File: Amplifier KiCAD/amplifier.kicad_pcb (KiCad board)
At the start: 2 copper layers, 197 parts, among them J1 Conn_01x03_Pin, J10 PA_IN, J11 EQ_OUT, J12 Speakers, J2 Main Power In, J3 LCD I2C, J4 Fan Tach and PWM, J5 Fan Power and GND, J6 VP and VN, J7 DEBUG, J8 Power To Amp, J9 Power In, Q1 BC546, Q10 TIP36, Q11 BC546, Q12 BCM846BS-7, Q13 BC546, Q14 BC546, Q15 BD140, Q16 BC546, Q17 BD139, Q18 BD140, Q19 TIP36, Q2 BC546, Q20 TIP35, Q21 2N3904, Q22 2N7002, Q3 BCM846BS-7, Q4 BC546, Q5 BD140, Q6 BC546, Q7 BD140, Q8 TIP35, Q9 BD139, SW1 SW_Push, U1 TL081, U10 LM317_TO-220, U11 LM337_TO220, U12 STM32G031K8Tx, U2 TL081, U3 TL081, U4 TL081, U5 TL081, U6 TL081, U7 LMR36520FADDAR, U8 LMR36520FADDAR, U9 TLV75533PDBVR

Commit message: Component Placement Finalised, Starting Traces
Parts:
- removed Q12, Q3: BCM846BS-7, Package_TO_SOT_SMD:SOT-363_SC-70-6
- added Q23: BCM846BS-7, Package_TO_SOT_SMD:SOT-363_SC-70-6, F.Cu at (103.5, -152.4)
- added Q24: BCM846BS-7, Package_TO_SOT_SMD:SOT-363_SC-70-6, F.Cu at (100.8, -116.2)
- added REF**: MountingHole_3.2mm_M3, MountingHole:MountingHole_3.2mm_M3, F.Cu at (330.8, -118.7)
- added REF**: MountingHole_3.2mm_M3, MountingHole:MountingHole_3.2mm_M3, F.Cu at (228.0, -81.3)
- added REF**: MountingHole_3.2mm_M3, MountingHole:MountingHole_3.2mm_M3, F.Cu at (330.8, -87.6)
- added REF**: MountingHole_3.2mm_M3, MountingHole:MountingHole_3.2mm_M3, F.Cu at (69.8, -172.7)
- added REF**: MountingHole_3.2mm_M3, MountingHole:MountingHole_3.2mm_M3, F.Cu at (515.0, -118.7)
- added REF**: MountingHole_3.2mm_M3, MountingHole:MountingHole_3.2mm_M3, F.Cu at (228.0, -172.1)
- added REF**: MountingHole_3.2mm_M3, MountingHole:MountingHole_3.2mm_M3, F.Cu at (69.8, -81.3)
- added REF**: MountingHole_3.2mm_M3, MountingHole:MountingHole_3.2mm_M3, F.Cu at (515.0, -87.6)
- J5: footprint Connector_Molex:Molex_Micro-Fit_3.0_43045-0812_2x04_P3.00mm_Vertical -> KiCADModels:Molex_Micro-Fit_3.0_43045-0812_2x04_P3.00mm_Vertical
- moved RV8 466.1 mm to (463.4, -90.3), turned to 90 degrees
- moved J4 438.5 mm to (480.3, -116.8)
- moved RV7 437.1 mm to (436.1, -90.3), turned to 90 degrees
- moved J5 428.0 mm to (461.7, -117.0)
- moved RV6 410.0 mm to (410.8, -90.3), turned to 90 degrees
- moved RV5 381.1 mm to (383.5, -90.3), turned to 90 degrees
- moved J8 355.1 mm to (378.0, -120.8), turned to 180 degrees
- moved J1 322.7 mm to (354.8, -85.1), turned to 90 degrees
- moved J12 282.3 mm to (225.1, -125.7), turned to 90 degrees
- moved R27 268.0 mm to (175.9, -161.9), turned to 90 degrees
- moved J10 262.3 mm to (76.8, -150.9), turned to 90 degrees
- moved Q8 260.1 mm to (184.0, -172.5), turned to -90 degrees
- moved C11 257.4 mm to (-92.0, 97.3)
- moved C12 257.4 mm to (-92.0, 100.2)
- moved C18 257.4 mm to (-81.9, 131.5)
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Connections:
- R20 pad 2: VCC -> Net-(Q10-E)
- R35 pad 2: VCC -> Net-(Q14-C)
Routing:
- net Out+: track 0.00 -> 137.4 mm
- net VCC: track 0.00 -> 69.9 mm
- net Net-(Q1-C): track 0.00 -> 35.0 mm
- net VEE: track 0.00 -> 33.3 mm
- net Net-(Q6-E): track 0.00 -> 29.8 mm
- net Net-(Q2-B): track 0.00 -> 24.8 mm
- net Net-(Q23B-C2): track 0.00 -> 22.8 mm
- net Net-(Q14-B): track 0.00 -> 22.5 mm
- net Net-(Q13-B): track 0.00 -> 22.3 mm
- net Net-(Q5-C): track 0.00 -> 20.2 mm
- net Net-(C29-Pad2): track 0.00 -> 20.1 mm
- net Net-(Q6-B): track 0.00 -> 18.8 mm
- net Net-(Q23A-E1): track 0.00 -> 18.7 mm, vias 0 -> 3
- net In+: track 0.00 -> 17.9 mm
- net Net-(C39-Pad2): track 0.00 -> 17.3 mm
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- added copper zone on In1.Cu, net Net-(Q10-E)
- added copper zone on In1.Cu, net Net-(Q14-C)
- added copper zone on In2.Cu, net Net-(Q20-E)
- added copper zone on In2.Cu, net Net-(Q23A-E1)
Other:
- board outline added: 454.3 x 100.3 mm
- copper layers 2 -> 4

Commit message: Save Before big changes
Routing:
- net Out+: track 137.4 -> 0.00 mm
- net VCC: track 69.9 -> 0.00 mm
- net Net-(Q1-C): track 35.0 -> 0.00 mm
- net VEE: track 33.3 -> 0.00 mm
- net Net-(Q6-E): track 29.8 -> 0.00 mm
- net Net-(Q2-B): track 24.8 -> 0.00 mm
- net Net-(Q23B-C2): track 22.8 -> 0.00 mm
- net Net-(Q14-B): track 22.5 -> 0.00 mm
- net Net-(Q13-B): track 22.3 -> 0.00 mm
- net Net-(Q5-C): track 20.2 -> 0.00 mm
- net Net-(C29-Pad2): track 20.1 -> 0.00 mm
- net Net-(Q6-B): track 18.8 -> 0.00 mm
- net Net-(Q23A-E1): track 18.7 -> 0.00 mm, vias 3 -> 0
- net In+: track 17.9 -> 0.00 mm
- net Net-(C39-Pad2): track 17.3 -> 0.00 mm
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
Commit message: Save before KiCAD update
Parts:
- moved J11 524.9 mm to (383.1, -118.9)
- moved C27 295.3 mm to (123.6, 149.6), turned to 90 degrees
- moved R16 290.4 mm to (118.4, 150.0), turned to 90 degrees
- moved R15 285.6 mm to (113.5, 139.8), turned to -90 degrees
- moved U11 284.7 mm to (102.7, 146.1)
- moved D3 280.7 mm to (108.2, 154.6), turned to 180 degrees
- moved D4 280.1 mm to (108.2, 149.7), turned to 180 degrees
- moved C23 279.0 mm to (116.3, 152.9), turned to 180 degrees
- moved C26 261.2 mm to (89.5, 154.6)
- moved C22 254.9 mm to (92.3, 151.4)
- moved RFBT2 235.4 mm to (137.3, 100.5), turned to 180 degrees
- moved C17 235.3 mm to (37.5, 82.0)
- moved C20 235.3 mm to (18.0, 96.2)
- moved C21 235.3 mm to (37.5, 84.9)
- moved C24 235.3 mm to (28.4, 82.5)
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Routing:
- net GND: track 0.00 -> 279.8 mm
- net VCC: track 0.00 -> 218.7 mm
- net Net-(Q14-C): track 0.00 -> 197.1 mm
- net Net-(Q23A-E1): track 0.00 -> 194.4 mm, vias 0 -> 3
- net VEE: track 0.00 -> 168.9 mm
- net Net-(Q20-E): track 0.00 -> 168.7 mm, vias 0 -> 2
- net Net-(Q10-E): track 0.00 -> 148.4 mm
- net Out+: track 0.00 -> 118.1 mm
- net Out-: track 0.00 -> 114.0 mm
- net Net-(Q17-E): track 0.00 -> 57.5 mm
- net Net-(Q10-C): track 0.00 -> 53.4 mm
- net Net-(Q18-C): track 0.00 -> 50.7 mm
- net Net-(Q10-B): track 0.00 -> 50.5 mm
- net Net-(Q17-C): track 0.00 -> 48.4 mm
- net Net-(Q18-E): track 0.00 -> 44.5 mm
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- removed copper zone on In1.Cu, net Net-(Q10-E)
- removed copper zone on In1.Cu, net Net-(Q14-C)
- removed copper zone on In2.Cu, net Net-(Q20-E)
- removed copper zone on In2.Cu, net Net-(Q23A-E1)

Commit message: Completed placement of equaliser; Tidied up soldermask; Started STM32 placement
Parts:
- moved R12 615.8 mm to (402.6, 76.8), turned to 180 degrees
- moved R11 606.0 mm to (391.8, 61.6)
- moved R9 583.9 mm to (370.4, 61.2), turned to -90 degrees
- moved R10 580.1 mm to (367.1, 70.9), turned to 180 degrees
- moved U3 577.4 mm to (389.9, 72.9), turned to 180 degrees
- moved R7 556.5 mm to (343.3, 58.5), turned to -90 degrees
- moved C16 555.9 mm to (377.6, 71.2), turned to 90 degrees
- moved U6 554.5 mm to (401.7, 72.8), turned to 180 degrees
- moved R8 553.0 mm to (340.3, 68.3), turned to 180 degrees
- moved C13 552.9 mm to (365.5, 74.7)
- moved C14 551.9 mm to (373.9, 71.2), turned to 90 degrees
- moved C59 543.6 mm to (373.9, 58.1), turned to -90 degrees
- moved C9 534.2 mm to (346.9, 68.5), turned to 90 degrees
- moved C58 533.0 mm to (354.1, 71.0), turned to 90 degrees
- moved C10 533.0 mm to (345.8, 76.5), turned to 90 degrees
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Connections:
- RV5 pad 1: GND -> Net-(U3-+)
- RV5 pad 2: Bass -> Net-(C3-Pad2)
- RV5 pad 3: +3.3V -> Net-(U3--)
- RV5 pad 4: Net-(U3--) -> GND
- RV5 pad 5: Net-(C3-Pad2) -> Bass
- RV5 pad 6: Net-(U3-+) -> +3.3V
- RV6 pad 1: GND -> Net-(U3-+)
- RV6 pad 2: Mid -> Net-(C10-Pad1)
- RV6 pad 3: +3.3V -> Net-(U3--)
- RV6 pad 4: Net-(U3--) -> GND
- RV6 pad 5: Net-(C10-Pad1) -> Mid
- RV6 pad 6: Net-(U3-+) -> +3.3V
- RV7 pad 1: GND -> Net-(U3-+)
- RV7 pad 2: Treble -> Net-(C13-Pad1)
- RV7 pad 3: +3.3V -> Net-(U3--)
- RV7 pad 4: Net-(U3--) -> GND
- RV7 pad 5: Net-(C13-Pad1) -> Treble
- RV7 pad 6: Net-(U3-+) -> +3.3V
- RV8 pad 1: GND -> In+
- RV8 pad 2: Volume -> Net-(U3--)
- RV8 pad 3: +3.3V -> unconnected-(RV8-Pad3)
- RV8 pad 4: unconnected-(RV8-Pad4) -> +3.3V
- RV8 pad 5: Net-(U3--) -> Volume
- RV8 pad 6: In+ -> GND
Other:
- board size 454.3 x 100.3 mm -> 379.4 x 265.9 mm

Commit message: Started equaliser PCB traces, need to check trace widths all round
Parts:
- moved J7 386.9 mm to (218.8, -43.3), turned to 90 degrees
- moved C55 375.1 mm to (203.5, -28.9), turned to 180 degrees
- moved COUT4 353.2 mm to (202.4, -34.1), turned to 180 degrees
- moved J4 341.6 mm to (154.4, -42.4)
- moved Q21 337.6 mm to (141.2, -30.7)
- moved R52 332.7 mm to (196.3, -50.8), turned to 180 degrees
- moved J6 330.8 mm to (143.1, -38.9), turned to 180 degrees
- moved R47 328.2 mm to (147.8, -38.9), turned to -90 degrees
- moved R48 320.0 mm to (136.3, -38.5), turned to -90 degrees
- moved C50 309.4 mm to (192.4, -45.9)
- moved C51 309.4 mm to (196.3, -46.0)
- moved C52 309.4 mm to (199.9, -44.7)
- moved R49 309.4 mm to (209.2, -28.4)
- moved R50 309.4 mm to (212.9, -28.3)
- moved U12 309.4 mm to (207.5, -45.8)
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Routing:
- net +3.3V: track 0.00 -> 265.2 mm, vias 0 -> 1
- net +15V: track 0.00 -> 183.1 mm
- net GND: track 279.8 -> 456.1 mm
- net Net-(U12-PA8): track 0.00 -> 169.3 mm
- net -15V: track 0.00 -> 149.3 mm
- net Net-(U3-+): track 0.00 -> 147.5 mm
- net Bass: track 0.00 -> 145.3 mm
- net Net-(J3-Pin_1): track 0.00 -> 125.8 mm, vias 0 -> 1
- net Mid: track 0.00 -> 123.1 mm
- net Net-(J3-Pin_2): track 0.00 -> 119.7 mm, vias 0 -> 1
- net Net-(Q21-C): track 0.00 -> 118.4 mm
- net VCC: track 218.7 -> 335.6 mm
- net Net-(U3--): track 0.00 -> 97.2 mm
- net Treble: track 0.00 -> 90.3 mm
- net Net-(J4-Pin_5): track 0.00 -> 88.7 mm
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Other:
- board size 379.4 x 265.9 mm -> 167.5 x 204.9 mm

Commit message: Finished all traces and board shape
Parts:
- removed the REF** at (69.6, -67.9)
- moved R55 243.0 mm to (218.1, -225.8)
- moved R53 242.7 mm to (216.3, -239.0), turned to 90 degrees
- moved Q22 232.3 mm to (213.9, -234.4), turned to 0 degrees
- moved R54 225.8 mm to (209.8, -234.8)
- moved R50 210.7 mm to (212.7, -239.0)
- moved REF** 210.6 mm to (228.0, -187.4)
- moved REF** 210.6 mm to (70.0, -186.8)
- moved REF** 210.6 mm to (228.0, -278.5)
- moved C10 210.6 mm to (133.6, -195.1)
- moved C16 210.6 mm to (165.4, -200.5)
- moved C18 210.6 mm to (177.3, -228.6)
- moved C20 210.6 mm to (87.1, -226.3)
- moved C27 210.6 mm to (143.8, -225.3)
- moved C50 210.6 mm to (192.4, -256.5)
- moved C57 210.6 mm to (115.1, -203.1)
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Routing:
- net GND: track 456.1 -> 1123.0 mm, vias 0 -> 1
- net Net-(U12-PA8): track 169.3 -> 7.48 mm
- net VEE: track 187.6 -> 295.9 mm
- net +5V: track 27.0 -> 119.8 mm, vias 0 -> 2
- net VCC: track 335.6 -> 402.1 mm
- net Net-(J4-Pin_2): track 4.20 -> 62.6 mm
- net +3.3V: track 265.2 -> 300.8 mm
- net Net-(Q23A-E1): track 194.4 -> 160.3 mm
- net FAN POWER: track 37.1 -> 58.4 mm
- net Net-(J4-Pin_5): track 88.7 -> 67.6 mm
- net Net-(U7-FB): track 2.92 -> 12.3 mm, vias 0 -> 1
- net Net-(Q20-E): track 168.7 -> 175.4 mm
- net Net-(Q14-C): track 197.1 -> 191.1 mm
- net Net-(U8-SW): track 5.05 -> 11.0 mm
- net Net-(Q14-B): track 16.1 -> 21.2 mm
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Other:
- board size 167.5 x 204.9 mm -> 167.5 x 206.1 mm

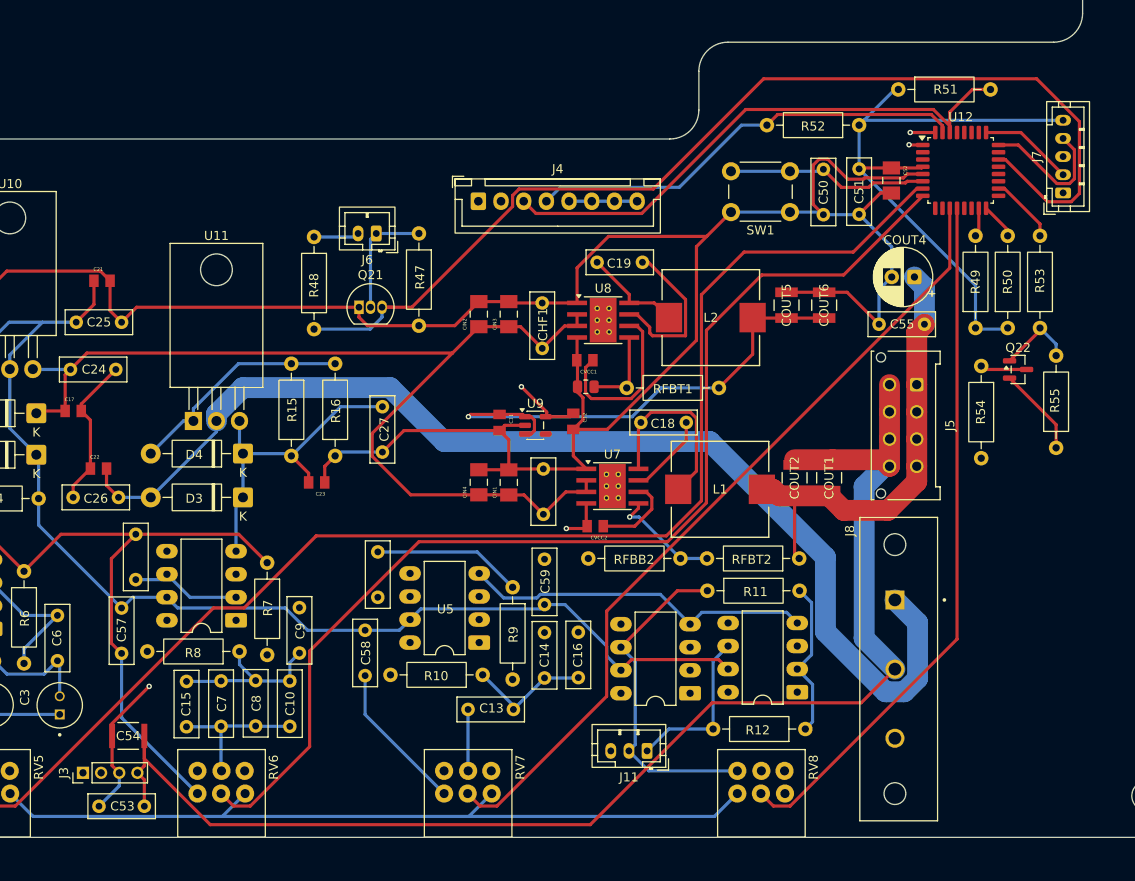
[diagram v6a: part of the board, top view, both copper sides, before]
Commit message: Added decoupling capacitors, finished traces, moved I2C jack closer to microcontroller. TODO: Check footprints a final time, check trace thickness, check capacitor locations
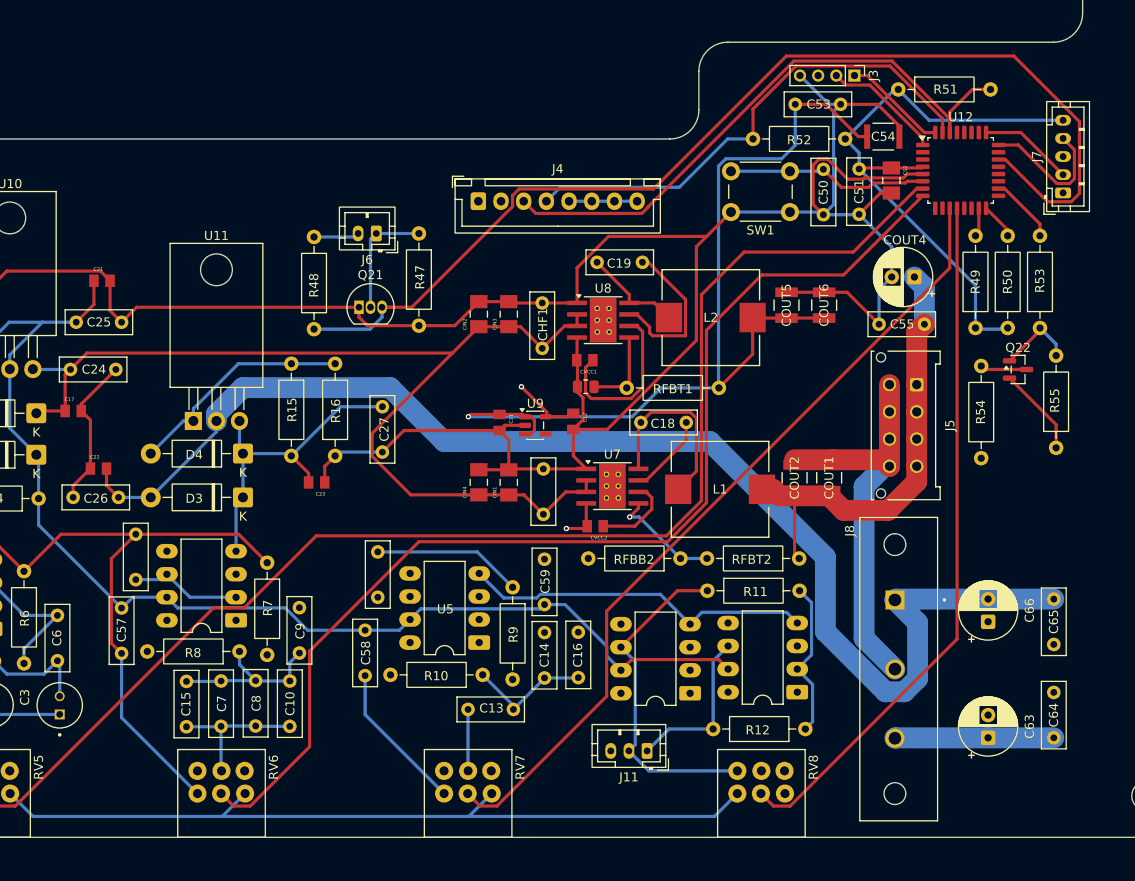
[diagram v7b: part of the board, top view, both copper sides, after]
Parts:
- added C63: 100u, Capacitor_THT:CP_Radial_D6.3mm_P2.50mm, F.Cu at (210.6, -193.8)
- added C64: 100n, Capacitor_THT:C_Rect_L7.2mm_W2.5mm_P5.00mm, F.Cu at (217.8, -198.8)
- added C65: 100n, Capacitor_THT:C_Rect_L7.2mm_W2.5mm_P5.00mm, F.Cu at (217.8, -209.1)
- added C66: 100u, Capacitor_THT:CP_Radial_D6.3mm_P2.50mm, F.Cu at (210.6, -206.6)
- moved J3 114.6 mm to (195.8, -266.8), turned to -90 degrees
- moved C53 109.0 mm to (189.3, -263.7)
- moved C54 106.2 mm to (199.0, -260.1)
- moved R52 2.15 mm to (194.8, -259.8)
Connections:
- RV8 pad 4: +3.3V -> GND
- RV8 pad 6: GND -> +3.3V
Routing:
- net Net-(J3-Pin_1): track 125.8 -> 11.5 mm, vias 1 -> 0
- net Net-(J3-Pin_2): track 119.7 -> 13.2 mm, vias 1 -> 0
- net GND: track 1123.0 -> 1083.3 mm
- net VEE: track 295.9 -> 313.4 mm
- net VCC: track 402.1 -> 419.6 mm
- net +5V: track 119.8 -> 108.1 mm, vias 2 -> 1
- net Net-(J4-Pin_4): track 48.9 -> 55.7 mm
- net Net-(J4-Pin_3): track 61.5 -> 66.4 mm
- net Net-(Q21-C): track 119.4 -> 121.4 mm
- net +3.3V: track 300.8 -> 299.0 mm
